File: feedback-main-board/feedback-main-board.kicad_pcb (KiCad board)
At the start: 4 copper layers, 80 x 64 mm, 88 parts, among them J1 908140508, J2 FLIP, J3 RPT, Q1 MMFTP3401, Q2 MMBT3904, Q3 MMBT3904, Q4 MMBT3904, SW1 SW_SPDT, SW2 SW_SPDT, U1 TL074, U2 TL074, U3 DG403, U4 NE555P, U5 4070

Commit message: Component placement
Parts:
- C1, C10, C11, C12, C13, C14, C15, C16, C17, C18, C19, C2, C20, C21, C22, C4, C5, C6, C7, C8, C9, D1, D2, D3, D4, D5, J1, J2, J3, Q1, Q2, Q3, Q4, R1, R10, R11, R12, R13, R14, R15, R16, R17, R18, R19, R2, R20, R21, R22, R23, R24, R25, R26, R27, R28, R29, R3, R30, R31, R32, R33, R34, R35, R36, R37, R38, R39, R4, R5, R6, R7, R8, R9, U1, U3, U4, U5: moved to B.Cu
- C3: footprint Capacitor_SMD:CP_Elec_4x5.4 -> Capacitor_SMD:CP_Elec_5x5.4; moved to B.Cu
- moved Q1 223.8 mm to (74.2, 123.4), turned to -90 degrees
- moved R1 220.8 mm to (70.5, 124.3), turned to 90 degrees
- moved D1 218.3 mm to (73.9, 119.9), turned to 180 degrees
- moved C1 196.1 mm to (81.3, 120.5), turned to -90 degrees
- moved R16 177.1 mm to (77.7, 100.1), turned to -90 degrees
- moved R11 176.9 mm to (77.5, 93.6), turned to -90 degrees
- moved C10 168.6 mm to (74.9, 100.1), turned to -90 degrees
- moved R35 167.0 mm to (61.5, 127.8), turned to -90 degrees
- moved R14 166.6 mm to (80.4, 103.9), turned to 90 degrees
- moved C12 166.4 mm to (89.4, 116.7)
- moved R4 165.8 mm to (119.4, 96.0), turned to 90 degrees
- moved R3 164.0 mm to (125.0, 96.0), turned to -90 degrees
- moved R30 163.6 mm to (70.5, 120.5), turned to 90 degrees
- moved R20 163.5 mm to (98.3, 109.7), turned to 90 degrees
- moved C4 162.6 mm to (116.7, 96.0), turned to 90 degrees
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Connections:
- U1 pad 1: Net-(R9-Pad1) -> Net-(R27-Pad1)
- U1 pad 10: Net-(C2-Pad1) -> Net-(C5-Pad2)
- U1 pad 12: Net-(R23-Pad2) -> Net-(C2-Pad1)
- U1 pad 13: Net-(R27-Pad1) -> Net-(R4-Pad1)
- U1 pad 14: Net-(R27-Pad1) -> Net-(R4-Pad1)
- U1 pad 2: Net-(R9-Pad1) -> Net-(R27-Pad1)
- U1 pad 3: Net-(C5-Pad2) -> Net-(R23-Pad2)
- U1 pad 8: Net-(R4-Pad1) -> Net-(R9-Pad1)
- U1 pad 9: Net-(R4-Pad1) -> Net-(R9-Pad1)
- U2 pad 1: Net-(R10-Pad1) -> Net-(C11-Pad2)
- U2 pad 10: /Core/RetBuf -> /+4V5
- U2 pad 12: /+4V5 -> /Core/RetBuf
- U2 pad 13: Net-(C10-Pad1) -> Net-(R11-Pad1)
- U2 pad 14: Net-(C10-Pad2) -> Net-(R11-Pad1)
- U2 pad 2: Net-(R10-Pad1) -> Net-(C11-Pad1)
- U2 pad 3: Net-(C6-Pad2) -> Net-(SW1-Pad2)
- U2 pad 5: Net-(SW1-Pad2) -> Net-(C6-Pad2)
- U2 pad 6: Net-(C11-Pad1) -> Net-(R10-Pad1)
- U2 pad 7: Net-(C11-Pad2) -> Net-(R10-Pad1)
- U2 pad 8: Net-(R11-Pad1) -> Net-(C10-Pad2)
- U2 pad 9: Net-(R11-Pad1) -> Net-(C10-Pad1)

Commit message: Routing v1 done
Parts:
- C5: footprint Capacitor_SMD:C_0603_1608Metric_Pad1.08x0.95mm_HandSolder -> Capacitor_THT:C_Rect_L7.0mm_W2.5mm_P5.00mm
- FLP: renamed from Ref**; value Val** -> FLP
- RPT: renamed from Ref**; value Val** -> RPT
- moved C13 9.91 mm to (112.7, 89.9)
- moved C7 9.54 mm to (112.7, 99.6), turned to 180 degrees
- moved C5 5.32 mm to (123.7, 104.9), turned to 0 degrees
- moved R5 2.79 mm to (122.2, 99.8)
- moved R9 2.67 mm to (119.4, 99.8)
- moved C1 1.91 mm to (83.2, 120.5)
- moved C17 1.91 mm to (69.2, 114.6)
- moved C22 1.91 mm to (63.6, 114.3)
- moved D1 1.91 mm to (75.8, 119.9)
- moved R1 1.91 mm to (72.4, 124.3)
- moved R30 1.91 mm to (72.4, 120.5)
- moved U4 1.91 mm to (74.9, 115.6)
- moved U5 1.91 mm to (66.2, 121.0)
- moved Q1 1.90 mm to (76.1, 123.4)
- moved R24 1.21 mm to (112.1, 123.5)
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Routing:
- net /+9V: track 0.00 -> 247.7 mm, vias 0 -> 14
- net /Core/OutPreVol: track 0.00 -> 125.7 mm
- net /Core/FxOut: track 0.00 -> 112.2 mm, vias 0 -> 4
- net /GND: track 0.00 -> 104.1 mm, vias 0 -> 58
- net /Switching/LatchState: track 0.00 -> 94.3 mm, vias 0 -> 2
- net /Core/InGain: track 0.00 -> 92.3 mm
- net /Core/RetBuf: track 0.00 -> 69.4 mm, vias 0 -> 3
- net /Switching/BypassState: track 0.00 -> 62.8 mm, vias 0 -> 4
- net /LatchSw1: track 0.00 -> 62.3 mm, vias 0 -> 5
- net Net-(R23-Pad2): track 0.00 -> 61.8 mm, vias 0 -> 2
- net Net-(R32-Pad2): track 0.00 -> 59.8 mm, vias 0 -> 2
- net Net-(SW1-Pad2): track 0.00 -> 52.1 mm, vias 0 -> 2
- net /Core/Feedback: track 0.00 -> 50.3 mm
- net Net-(R22-Pad2): track 0.00 -> 49.3 mm
- net /In: track 0.00 -> 48.8 mm, vias 0 -> 1
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- added copper zone on B.Cu, net /+4V5
- added copper zone on F.Cu, net /+4V5
- added copper zone on In1.Cu, net /GND
- added copper zone on In2.Cu, net /GND

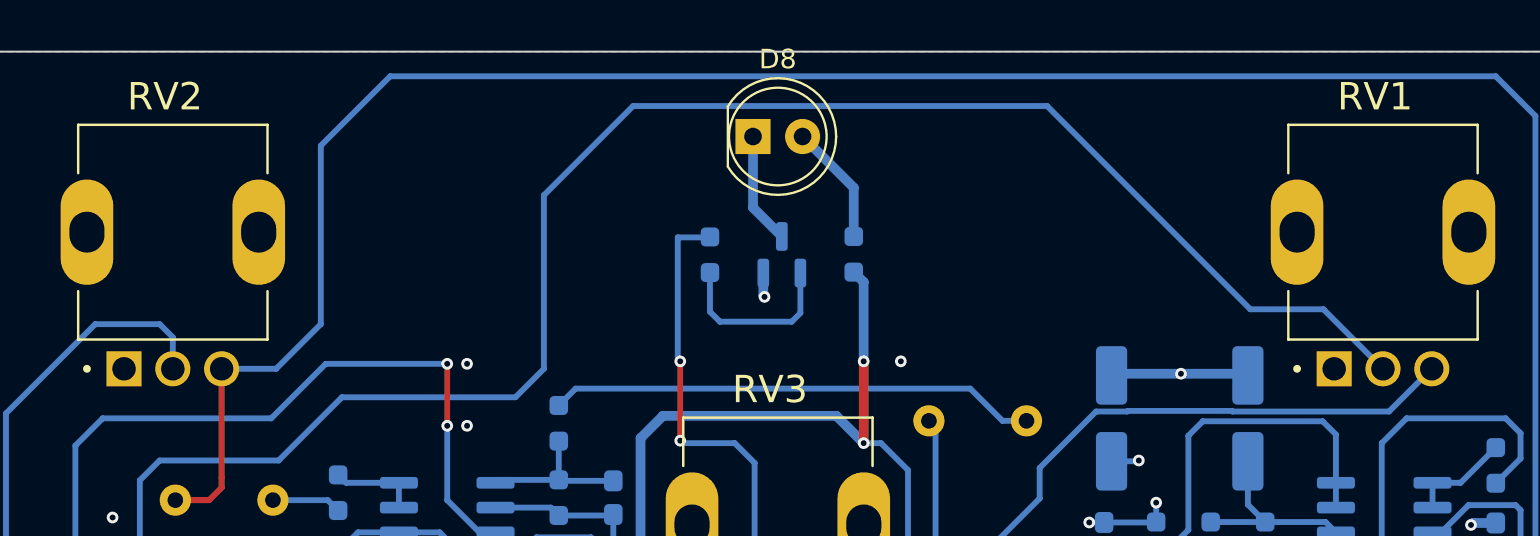
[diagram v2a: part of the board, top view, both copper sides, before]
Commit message: Rotate molex connector properly
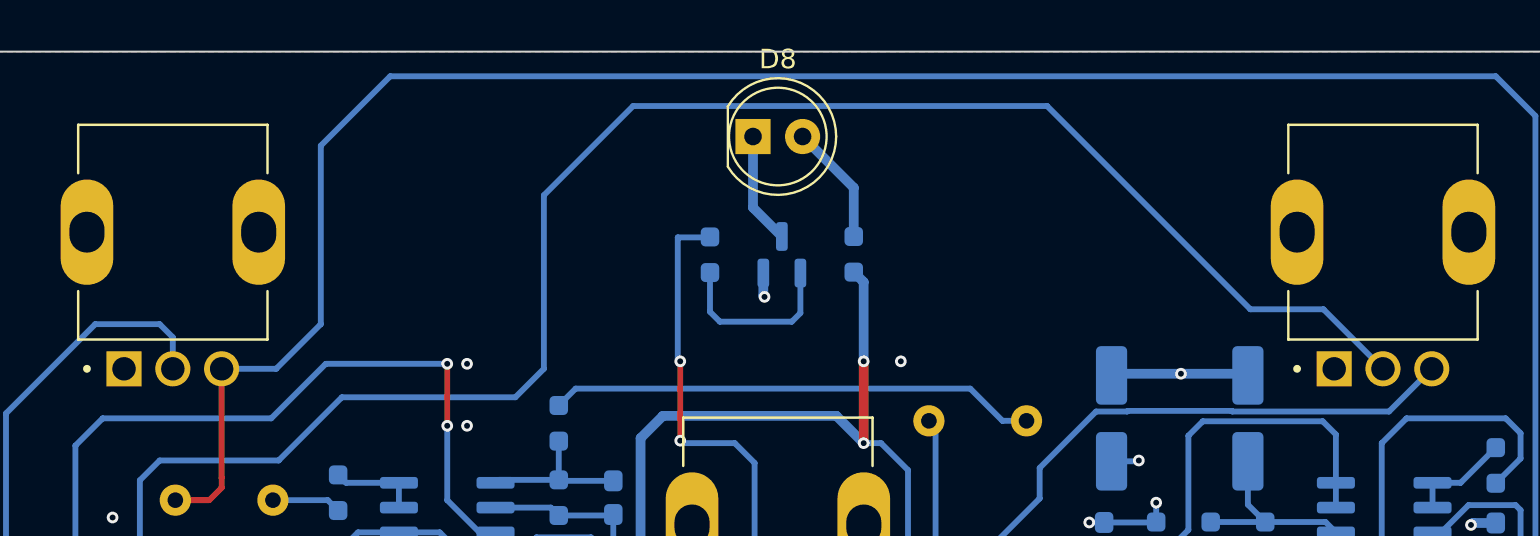
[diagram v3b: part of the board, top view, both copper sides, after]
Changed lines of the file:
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@@
     (property "Sheetname" "Core")
     (attr through_hole)
-    (fp_text reference "RV2" (at -0.405 -6.939) (layer "F.SilkS")
+    (fp_text reference "RV2" (at -0.405 -6.939) (layer "F.SilkS") hide
       (effects (font (size 1.4 1.4) (thickness 0.15)))
     )
@@
     (property "Sheetname" "Core")
     (attr through_hole)
-    (fp_text reference "RV3" (at -0.405 -6.939) (layer "F.SilkS")
+    (fp_text reference "RV3" (at -0.405 -6.939) (layer "F.SilkS") hide
       (effects (font (size 1.4 1.4) (thickness 0.15)))
     )
@@
     (property "Sheetname" "Core")
     (attr through_hole)
-    (fp_text reference "RV1" (at -0.405 -6.939) (layer "F.SilkS")
+    (fp_text reference "RV1" (at -0.405 -6.939) (layer "F.SilkS") hide
       (effects (font (size 1.4 1.4) (thickness 0.15)))
     )
@@
     (pad "8" smd rect locked (at 4.445 3.001902) (size 1.1938 2.0066) (layers "B.Cu" "B.Paste" "B.Mask")
       (net 2 "/GND") (pinfunction "8") (pintype "unspecified"))
+    (model "/Volumes/hdd/Projects/kicad/footprints/molex/ul_908140508/908140508.stp"
+      (offset (xyz 0 0 0))
+      (scale (xyz 1 1 1))
+      (rotate (xyz 0 0 0))
+    )
   )
   (footprint "Package_SO:SOIC-16_3.9x9.9mm_P1.27mm" (layer "B.Cu")

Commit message: Main PCB done
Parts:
- added kibuzzard-67A4EAB6: G***, kibuzzard-67A4EAB6, F.Cu at (79.8, 80.3)
- added kibuzzard-67A4EAD0: G***, kibuzzard-67A4EAD0, F.Cu at (118.7, 80.3)
- added kibuzzard-67A4EB37: G***, kibuzzard-67A4EB37, F.Cu at (100.1, 86.7)
- added kibuzzard-67A4EB98: G***, kibuzzard-67A4EB98, F.Cu at (130.9, 114.9)
- added kibuzzard-67A4EBC1: G***, kibuzzard-67A4EBC1, F.Cu at (69.0, 114.9)
- added kibuzzard-67A4EC3B: G***, kibuzzard-67A4EC3B, B.Cu at (85.0, 80.3)
- added kibuzzard-67A4EC49: G***, kibuzzard-67A4EC49, B.Cu at (114.4, 80.3)
- added kibuzzard-67A4ED41: G***, kibuzzard-67A4ED41, B.Cu at (100.0, 133.5)
- added kibuzzard-67A4EDCC: G***, kibuzzard-67A4EDCC, B.Cu at (100.0, 73.0)
- moved Q1 1.02 mm to (76.1, 124.5)
- moved D1 0.63 mm to (76.2, 120.4)
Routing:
- net Net-(Q4-Pad1): track 9.08 -> 7.25 mm
- net /Core/FxOut: track 112.2 -> 113.9 mm
- net Net-(SW1-Pad2): track 52.1 -> 53.5 mm
- net /Core/Sum: track 20.6 -> 19.7 mm
- net /Snd: track 40.7 -> 39.9 mm
- net /LatchSw1: track 62.3 -> 61.7 mm
- net /Core/OutPreVol: track 125.7 -> 125.1 mm
- net /GND: track 104.1 -> 104.3 mm, vias 58 -> 80
- net /+4V5: track 13.3 -> 13.4 mm, vias 10 -> 29

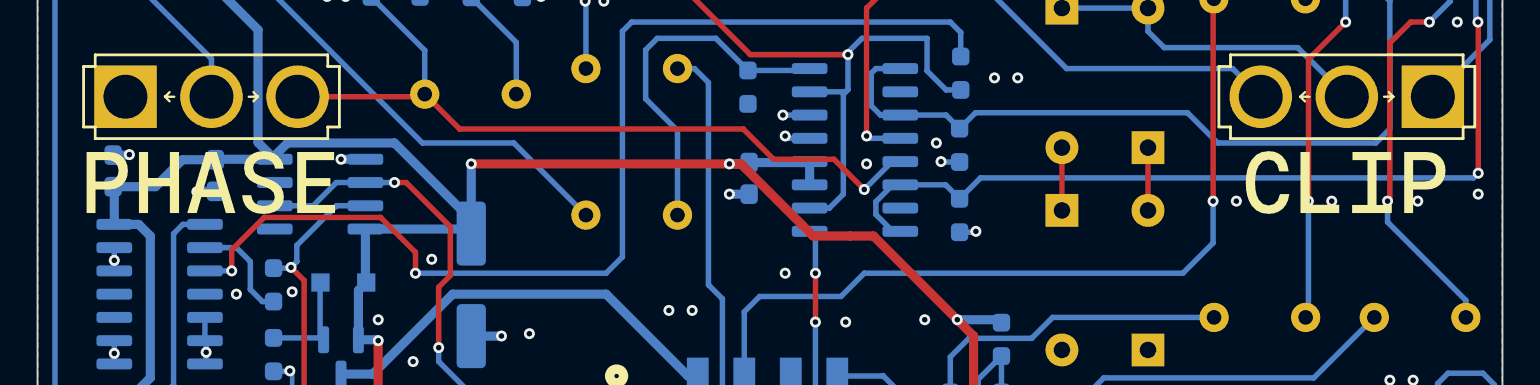
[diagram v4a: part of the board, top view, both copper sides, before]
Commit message: Main v1rev1 ordered at Aisler
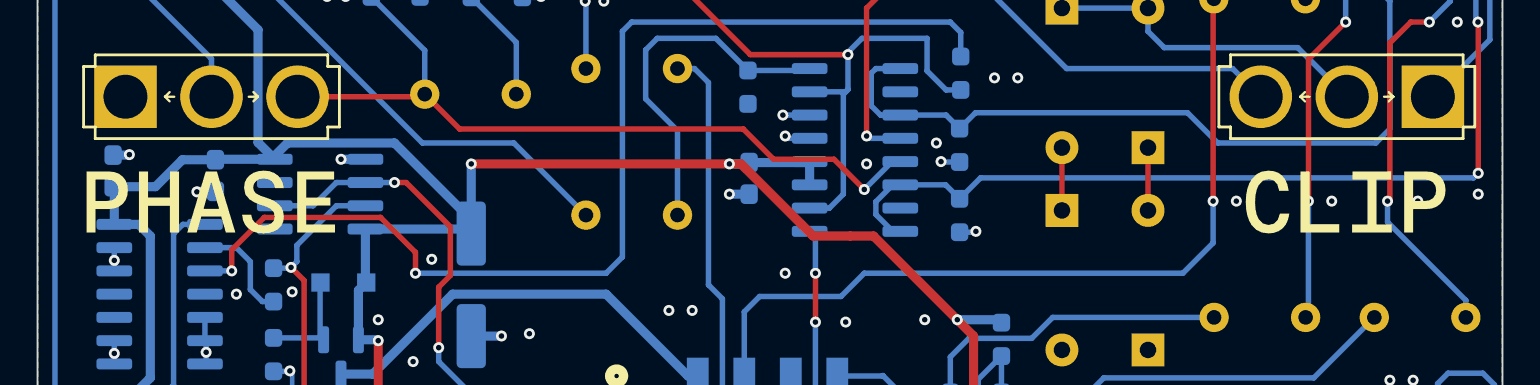
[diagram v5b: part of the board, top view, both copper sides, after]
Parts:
- moved kibuzzard-67A4EB98 1.06 mm to (130.9, 116.0)
- moved kibuzzard-67A4EBC1 1.06 mm to (69.0, 116.0)
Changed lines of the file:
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@@
   )
   (footprint "kibuzzard-67A4EB98" (layer "F.Cu")
-    (at 130.937 114.935)
+    (at 130.937 116)
     (descr "Generated with KiBuzzard")
     (tags "kb_params=eyJBbGlnbm1lbnRDaG9pY2UiOiAiQ2VudGVyIiwgIkNhcExlZnRDaG9pY2UiOiAiIiwgIkNhcFJpZ2h0Q2hvaWNlIjogIiIsICJGb250Q29tYm9Cb3giOiAiTW9kZXJhdC1Nb25vLU1lZGl1bSIsICJIZWlnaHRDdHJsIjogIjMiLCAiTGF5ZXJDb21ib0JveCI6ICJGLlNpbGtTIiwgIk11bHRpTGluZVRleHQiOiAiQ0xJUCIsICJQYWRkaW5nQm90dG9tQ3RybCI6ICI1IiwgIlBhZGRpbmdMZWZ0Q3RybCI6ICI1IiwgIlBhZGRpbmdSaWdodEN0cmwiOiAiNSIsICJQYWRkaW5nVG9wQ3RybCI6ICI1IiwgIldpZHRoQ3RybCI6ICIzIn0=")
     (attr board_only exclude_from_pos_files exclude_from_bom)
     (fp_text reference "kibuzzard-67A4EB98" (at 0 -4.7625) (layer "F.SilkS") hide
-      (effects (font (size 0 0)))
+      (effects (font (size 0 0) (thickness 0.15)))
     )
     (fp_text value "G***" (at 0 4.7625) (layer "F.SilkS") hide
-      (effects (font (size 0 0)))
+      (effects (font (size 0 0) (thickness 0.15)))
     )
     (fp_poly (pts
@@
   )
   (footprint "kibuzzard-67A4EBC1" (layer "F.Cu")
-    (at 68.961 114.935)
+    (at 68.961 116)
     (descr "Generated with KiBuzzard")
     (tags "kb_params=eyJBbGlnbm1lbnRDaG9pY2UiOiAiQ2VudGVyIiwgIkNhcExlZnRDaG9pY2UiOiAiIiwgIkNhcFJpZ2h0Q2hvaWNlIjogIiIsICJGb250Q29tYm9Cb3giOiAiTW9kZXJhdC1Nb25vLU1lZGl1bSIsICJIZWlnaHRDdHJsIjogIjMiLCAiTGF5ZXJDb21ib0JveCI6ICJGLlNpbGtTIiwgIk11bHRpTGluZVRleHQiOiAiUEhBU0UiLCAiUGFkZGluZ0JvdHRvbUN0cmwiOiAiNSIsICJQYWRkaW5nTGVmdEN0cmwiOiAiNSIsICJQYWRkaW5nUmlnaHRDdHJsIjogIjUiLCAiUGFkZGluZ1RvcEN0cmwiOiAiNSIsICJXaWR0aEN0cmwiOiAiMyJ9")
     (attr board_only exclude_from_pos_files exclude_from_bom)
     (fp_text reference "kibuzzard-67A4EBC1" (at 0 -4.7625) (layer "F.SilkS") hide
-      (effects (font (size 0 0)))
+      (effects (font (size 0 0) (thickness 0.15)))
     )
     (fp_text value "G***" (at 0 4.7625) (layer "F.SilkS") hide
-      (effects (font (size 0 0)))
+      (effects (font (size 0 0) (thickness 0.15)))
     )
     (fp_poly (pts
@@
     (attr board_only exclude_from_pos_files exclude_from_bom)
     (fp_text reference "kibuzzard-67A4EAD0" (at 0 -4.7625) (layer "F.SilkS") hide
-      (effects (font (size 0 0)))
+      (effects (font (size 0 0) (thickness 0.15)))
     )
     (fp_text value "G***" (at 0 4.7625) (layer "F.SilkS") hide
-      (effects (font (size 0 0)))
+      (effects (font (size 0 0) (thickness 0.15)))
     )
     (fp_poly (pts
@@
     (attr board_only exclude_from_pos_files exclude_from_bom)
     (fp_text reference "kibuzzard-67A4EAB6" (at 0 -4.7625) (layer "F.SilkS") hide
-      (effects (font (size 0 0)))
+      (effects (font (size 0 0) (thickness 0.15)))
     )
     (fp_text value "G***" (at 0 4.7625) (layer "F.SilkS") hide
-      (effects (font (size 0 0)))
+      (effects (font (size 0 0) (thickness 0.15)))
     )
     (fp_poly (pts
@@
     (attr board_only exclude_from_pos_files exclude_from_bom)
     (fp_text reference "kibuzzard-67A4EB37" (at 0 -4.714875) (layer "F.SilkS") hide
-      (effects (font (size 0 0)))
+      (effects (font (size 0 0) (thickness 0.15)))
     )
     (fp_text value "G***" (at 0 4.714875) (layer "F.SilkS") hide
-      (effects (font (size 0 0)))
+      (effects (font (size 0 0) (thickness 0.15)))
     )
     (fp_poly (pts
@@
     (attr board_only exclude_from_pos_files exclude_from_bom)
     (fp_text reference "kibuzzard-67A4EC49" (at 0 6.937375) (layer "B.SilkS") hide
-      (effects (font (size 0 0)) (justify mirror))
+      (effects (font (size 0 0) (thickness 0.15)) (justify mirror))
     )
     (fp_text value "G***" (at 0 -6.937375) (layer "B.SilkS") hide
-      (effects (font (size 0 0)) (justify mirror))
+      (effects (font (size 0 0) (thickness 0.15)) (justify mirror))
     )
     (fp_poly (pts
@@
     (attr board_only exclude_from_pos_files exclude_from_bom)
     (fp_text reference "kibuzzard-67A4ED41" (at 0 3.563937) (layer "B.SilkS") hide
-      (effects (font (size 0 0)) (justify mirror))
+      (effects (font (size 0 0) (thickness 0.15)) (justify mirror))
     )
     (fp_text value "G***" (at 0 -3.563938) (layer "B.SilkS") hide
-      (effects (font (size 0 0)) (justify mirror))
+      (effects (font (size 0 0) (thickness 0.15)) (justify mirror))
     )
     (fp_poly (pts
@@
     (attr board_only exclude_from_pos_files exclude_from_bom)
     (fp_text reference "kibuzzard-67A4EC3B" (at 0 6.937375) (layer "B.SilkS") hide
-      (effects (font (size 0 0)) (justify mirror))
+      (effects (font (size 0 0) (thickness 0.15)) (justify mirror))
     )
     (fp_text value "G***" (at 0 -6.937375) (layer "B.SilkS") hide
-      (effects (font (size 0 0)) (justify mirror))
+      (effects (font (size 0 0) (thickness 0.15)) (justify mirror))
     )
     (fp_poly (pts
@@
     (attr board_only exclude_from_pos_files exclude_from_bom)
     (fp_text reference "kibuzzard-67A4EDCC" (at 0 3.90525) (layer "B.SilkS") hide
-      (effects (font (size 0 0)) (justify mirror))
+      (effects (font (size 0 0) (thickness 0.15)) (justify mirror))
     )
     (fp_text value "G***" (at 0 -3.90525) (layer "B.SilkS") hide
-      (effects (font (size 0 0)) (justify mirror))
+      (effects (font (size 0 0) (thickness 0.15)) (justify mirror))
     )
     (fp_poly (pts

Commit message: Wip rev2
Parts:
- added C23: 100n, Capacitor_THT:C_Rect_L7.0mm_W2.5mm_P5.00mm, B.Cu at (132.5, 115.4)
- added C24: 100n, Capacitor_THT:C_Rect_L7.0mm_W2.5mm_P5.00mm, B.Cu at (123.7, 115.4)
- added R40: 100k, Resistor_SMD:R_0603_1608Metric_Pad0.98x0.95mm_HandSolder, B.Cu at (133.5, 103.5)
- added R41: 100k, Resistor_SMD:R_0603_1608Metric_Pad0.98x0.95mm_HandSolder, B.Cu at (136.8, 87.1)
- R24, R25: value 100k -> 10k
- turned R31 to 90 degrees
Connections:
- C20 pad 1: /Switching/MomState -> /MomSw1
- J2 pad 2: /+9V -> Net-(R31-Pad1)
- R31 pad 1: /Switching/MomState -> Net-(R31-Pad1)
- R31 pad 2: /MomSw1 -> /+9V
- R35 pad 1: /Switching/MomState -> /MomSw1
- R39 pad 1: /Switching/MomState -> /MomSw1
- SW1 pad 1: /+4V5 -> /Core/RetBuf
- SW1 pad 3: /Core/RetBuf -> /+4V5
- U1 pad 3: Net-(R23-Pad2) -> Net-(U1-Pad3)
- U1 pad 5: Net-(R22-Pad2) -> Net-(U1-Pad5)
- U5 pad 1: /Switching/MomState -> /MomSw1
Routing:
- net Net-(U1-Pad3): track 0.00 -> 52.9 mm, vias 0 -> 4
- net Net-(R23-Pad2): track 61.8 -> 22.9 mm, vias 2 -> 0
- net /MomSw1: track 5.49 -> 35.9 mm
- net /Switching/MomState: track 29.3 -> 0.00 mm
- net Net-(U1-Pad5): track 0.00 -> 22.7 mm
- net Net-(R22-Pad2): track 49.3 -> 34.4 mm
- net /Core/RetBuf: track 69.4 -> 80.5 mm
- net Net-(R31-Pad1): track 0.00 -> 7.99 mm
- net /GND: track 104.3 -> 109.5 mm, vias 80 -> 84
- net /In: track 48.8 -> 52.1 mm
- net /+9V: track 247.8 -> 244.8 mm
- net Net-(C18-Pad1): track 25.4 -> 28.0 mm
- net Net-(C19-Pad1): track 43.2 -> 44.8 mm
- net /+4V5: track 13.4 -> 14.6 mm, vias 29 -> 31
